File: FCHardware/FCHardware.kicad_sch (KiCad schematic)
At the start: 29 parts, among them J1 USB_B_Mini, P1 USB_C_Plug_USB2.0, Q1 MMBT2222A, Q2 MMBT2222A, SW1 SW_DPST_Custom_PIN, U1 ESP32-WROOM-32, U2 MIC5219-3.3YMM, U3 CP2104, U4 MCP73831-3-OT, U5 MPU-6050, U6 L293D, U7 L293D

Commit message: Added Power and Motor Management, Accelerator
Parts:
- added C10: 0.1uF, symbol Device:C
- added C11: 2.2nF, symbol Device:C
- added J2, J3, J4, J5: Conn_01x02, symbol Connector_Generic:Conn_01x02
- added R8, R9: 0R, symbol Device:R
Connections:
- net GND: now also U5.1 (CLKIN), U5.11 (FSYNC), U5.18 (GND), C10.2, C11.2, R8.2
- net VBUS: now also U5.13 (VDD), U5.8 (VLOGIC), R9.1
- net at U5.10 (REGOUT): now also C10.1
- net INT: now reaches U5.12 (INT)
- net at U5.20 (CPOUT): now also C11.1
- net SCL: now reaches U5.23 (SCL)
- net SDA: now reaches U5.24 (SDA)
- net AUX_SDA: now reaches U5.6 (AUX_DA)
- net AUX_SCL: now reaches U5.7 (AUX_CL)
- net ADD: now reaches U5.9 (AD0)
- net ADD: now also R8.1, R9.2
- new net M1+: J2.1 (Pin_1)
- new net M1-: J2.2 (Pin_2)
- new net M2+: J3.1 (Pin_1)
- new net M2-: J3.2 (Pin_2)
- new net M3+: J4.1 (Pin_1)
- new net M3-: J4.2 (Pin_2)
- new net M4+: J5.1 (Pin_1)
- new net M4-: J5.2 (Pin_2)
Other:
- moved on the sheet: C1, C2, C3, C4, C5, C6, C7, C8, C9, D1, J1, P1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

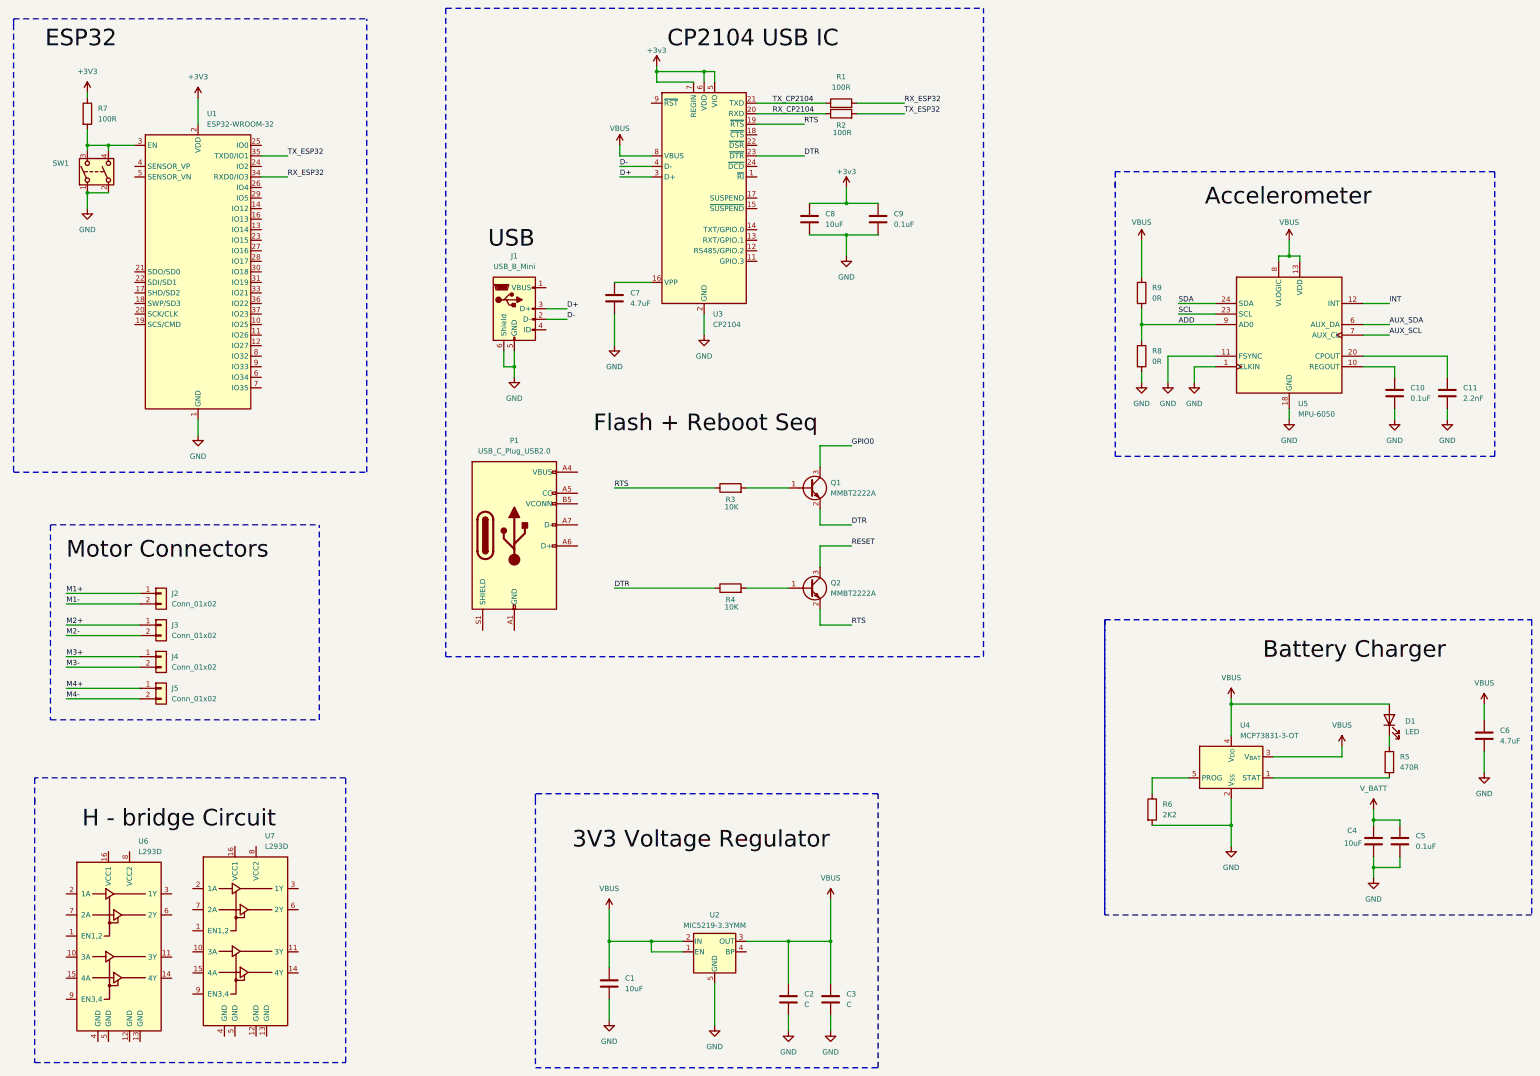
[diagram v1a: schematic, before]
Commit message: Changed main controller to Feather 32 and updated schematics accordingly
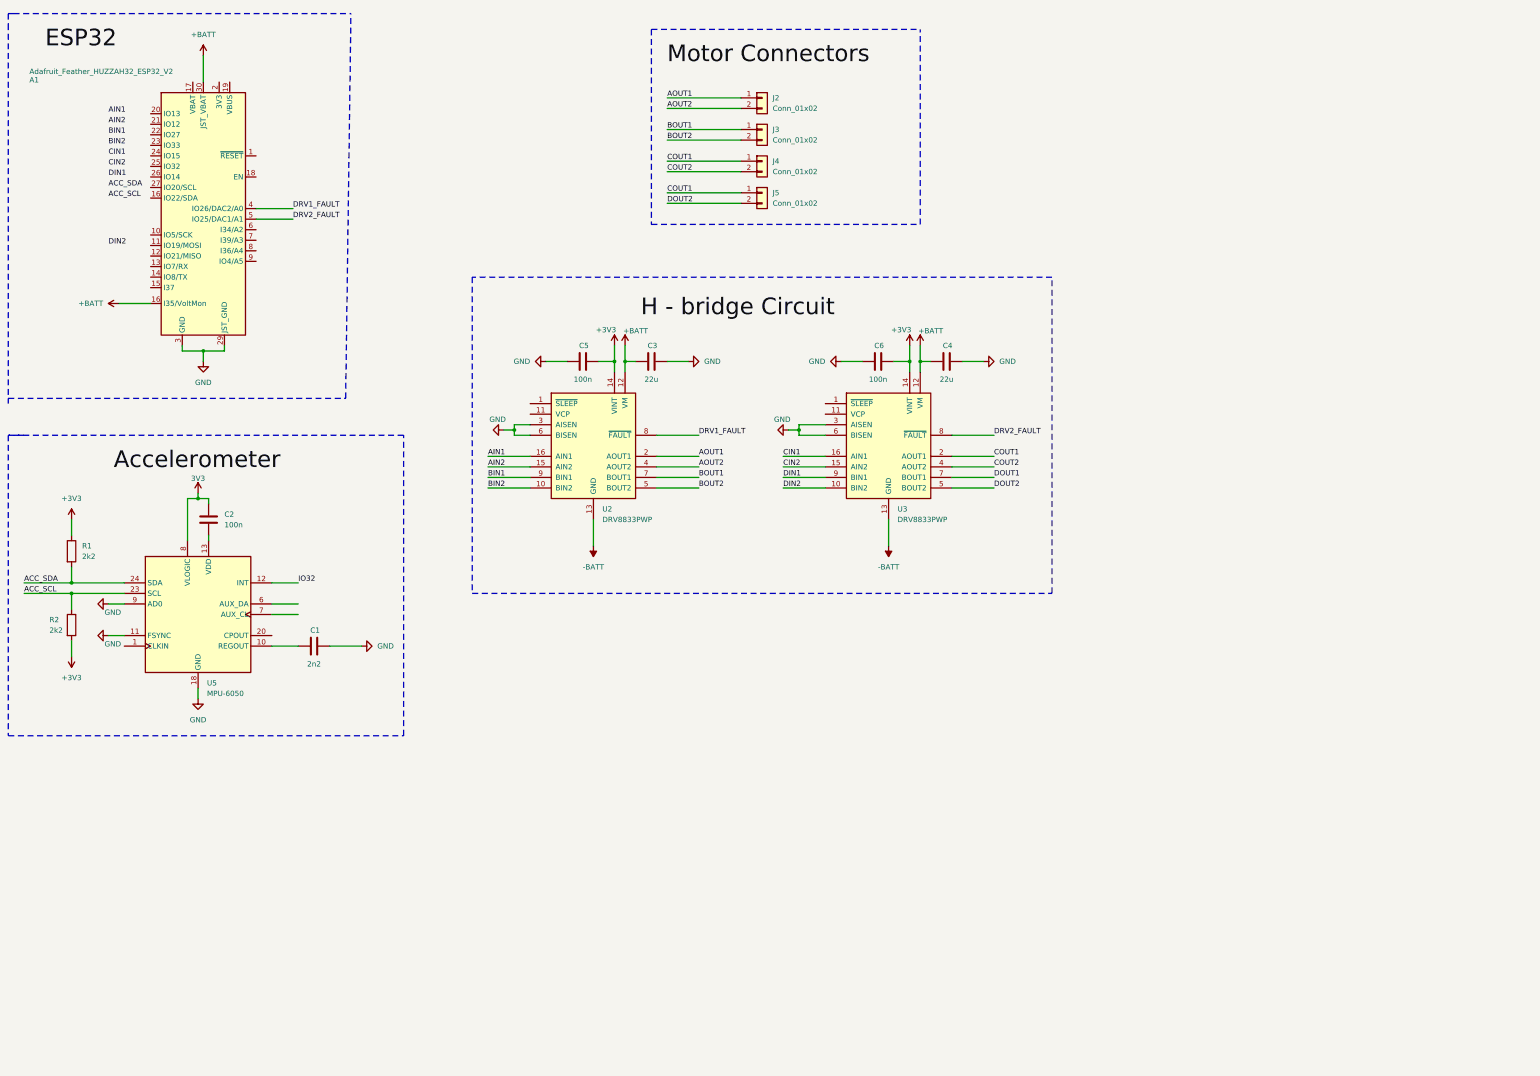
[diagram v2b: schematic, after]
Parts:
- removed C10, C9: 0.1uF, symbol Device:C
- removed C11: 2.2nF, symbol Device:C
- removed C7: 4.7uF, symbol Device:C
- removed C8: 10uF, symbol Device:C
- removed D1: LED, symbol Device:LED
- removed J1: USB_B_Mini, symbol Connector:USB_B_Mini
- removed P1: USB_C_Plug_USB2.0, symbol Connector:USB_C_Plug_USB2.0
- removed Q1, Q2: MMBT2222A, Package_TO_SOT_SMD:SOT-23, symbol Transistor_BJT:MMBT2222A
- removed R3, R4: 10K, symbol Device:R
- removed R5: 470R, symbol Device:R
- removed R6: 2K2, symbol Device:R
- removed R7: 100R, symbol Device:R
- removed R8, R9: 0R, symbol Device:R
- removed SW1: SW_DPST_Custom_PIN, symbol switches:SW_DPST_Custom_PIN
- removed U1: ESP32-WROOM-32, RF_Module:ESP32-WROOM-32, symbol RF_Module:ESP32-WROOM-32
- removed U2: MIC5219-3.3YMM, Package_SO:MSOP-8_3x3mm_P0.65mm, symbol Regulator_Linear:MIC5219-3.3YMM
- removed U3: CP2104, Package_DFN_QFN:QFN-24-1EP_4x4mm_P0.5mm_EP2.6x2.6mm, symbol Interface_USB:CP2104
- removed U4: MCP73831-3-OT, Package_TO_SOT_SMD:SOT-23-5, symbol Battery_Management:MCP73831-3-OT
- removed U6, U7: L293D, Package_DIP:DIP-16_W7.62mm, symbol Driver_Motor:L293D
- added A1: Adafruit_Feather_HUZZAH32_ESP32_V2, Module:Adafruit_Feather, symbol Custom_ESP32_Library:Adafruit_Feather_HUZZAH32_ESP32_v2
- added U2, U3: DRV8833PWP, Package_SO:HTSSOP-16-1EP_4.4x5mm_P0.65mm_EP3x3mm, symbol Driver_Motor:DRV8833PWP
- C1: value 10uF -> 2n2
- C2: value C -> 100n
- C3: value C -> 22u
- C4: value 10uF -> 22u
- C5: value 0.1uF -> 100n
- C6: value 4.7uF -> 100n
- R1, R2: value 100R -> 2k2
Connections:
- net ADD is gone; now on net GND: U5.9 (AD0)
- net M4+ is gone; now on net COUT1: J5.1 (Pin_1)
- net SCL is gone; now on net ACC_SCL: U5.23 (SCL)
- net SDA is gone; now on net ACC_SDA: U5.24 (SDA)
- net TX_CP2104 is gone; now on net +3V3: R1.1
- net TX_ESP32 is gone; now on net +3V3: R2.2
- net +3V3: now also C5.2, C6.2, U2.14 (VINT), U3.14 (VINT)
- net GND: now also C5.1, C6.1, A1.29 (JST_GND), A1.3 (GND), U2.3 (AISEN), U2.6 (BISEN), U3.3 (AISEN), U3.6 (BISEN); no longer C2.2, C5.2, C6.2, U5.1 (CLKIN)
- net at U5.10 (REGOUT): now also C1.1
- net AUX_SCL: no longer names the net of U5.7 (AUX_CL)
- net AUX_SDA: no longer names the net of U5.6 (AUX_DA)
- net INT renamed IO32
- net M1+ renamed AOUT1
- net AOUT1: now also U2.2 (AOUT1)
- net M1- renamed AOUT2
- net AOUT2: now also U2.4 (AOUT2)
- net M2+ renamed BOUT1
- net BOUT1: now also U2.7 (BOUT1)
- net M2- renamed BOUT2
- net BOUT2: now also U2.5 (BOUT2)
- net M3+ renamed COUT1
- net COUT1: now also U3.2 (AOUT1)
- net M3- renamed COUT2
- net COUT2: now also U3.4 (AOUT2)
- net M4- renamed DOUT2
- net DOUT2: now also U3.5 (BOUT2)
- net RX_CP2104 renamed ACC_SCL
- net RX_ESP32 renamed ACC_SDA
- removed net VBUS: C1.1, C2.1, C3.1, C6.1, U5.13 (VDD), U5.8 (VLOGIC)
- net V_BATT renamed +BATT
- net +BATT: now also C3.1, A1.16 (I35/VoltMon), A1.30 (JST_VBAT), U2.12 (VM), U3.12 (VM); no longer C5.1
- new net: C2.1, U5.13 (VDD)
- new net -BATT: U2.13 (GND), U2.17 (GND), U3.13 (GND), U3.17 (GND)
- new net 3V3: C2.2, U5.8 (VLOGIC)
- new net AIN1: U2.16 (AIN1)
- new net AIN2: U2.15 (AIN2)
- new net BIN1: U2.9 (BIN1)
- new net BIN2: U2.10 (BIN2)
- new net CIN1: U3.16 (AIN1)
- new net CIN2: U3.15 (AIN2)
- new net DIN1: U3.9 (BIN1)
- new net DIN2: U3.10 (BIN2)
- new net DOUT1: U3.7 (BOUT1)
- new net DRV1_FAULT: A1.4 (IO26/DAC2/A0), U2.8 (~{FAULT})
- new net DRV2_FAULT: A1.5 (IO25/DAC1/A1), U3.8 (~{FAULT})
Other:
- moved on the sheet: J2, J3, J4, J5, U5

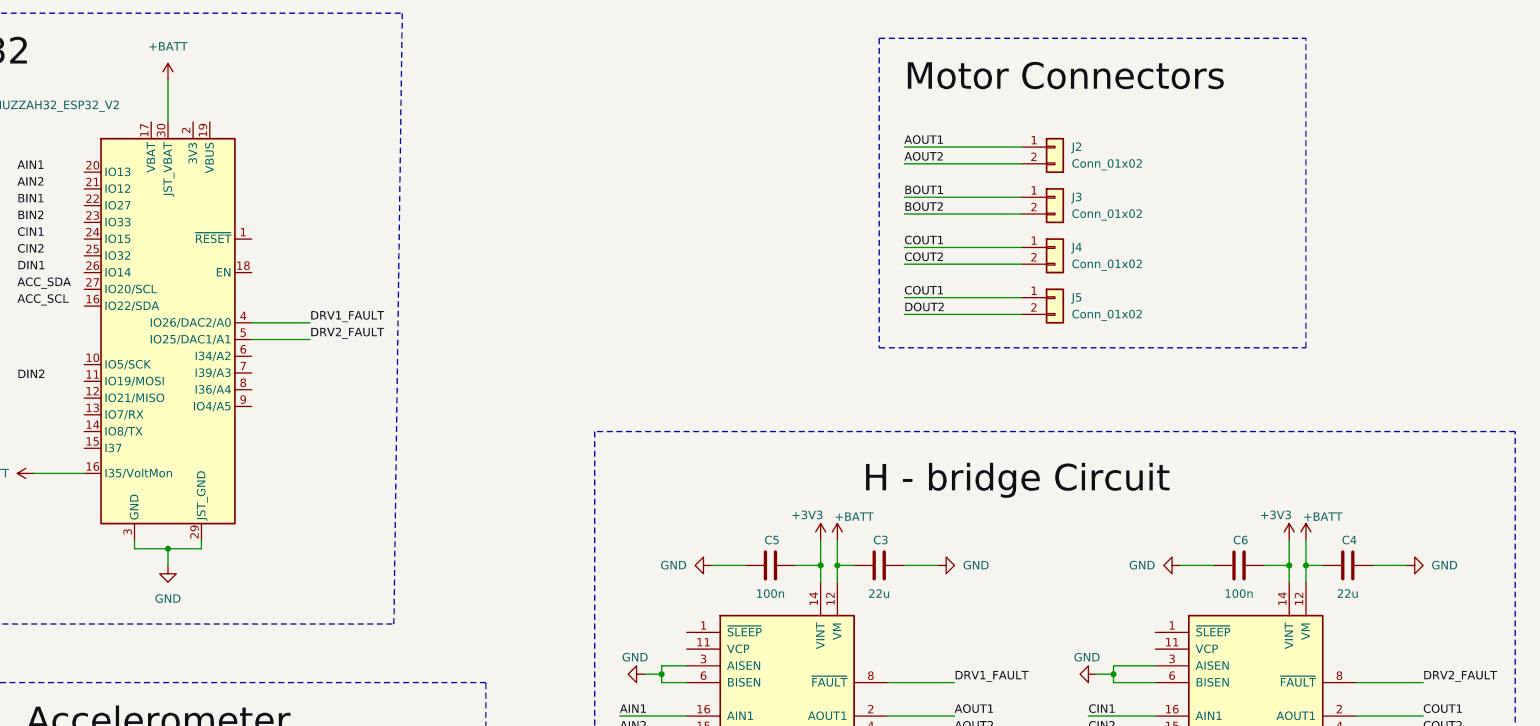
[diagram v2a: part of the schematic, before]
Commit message: Updated configuration to 2S LiPo battery
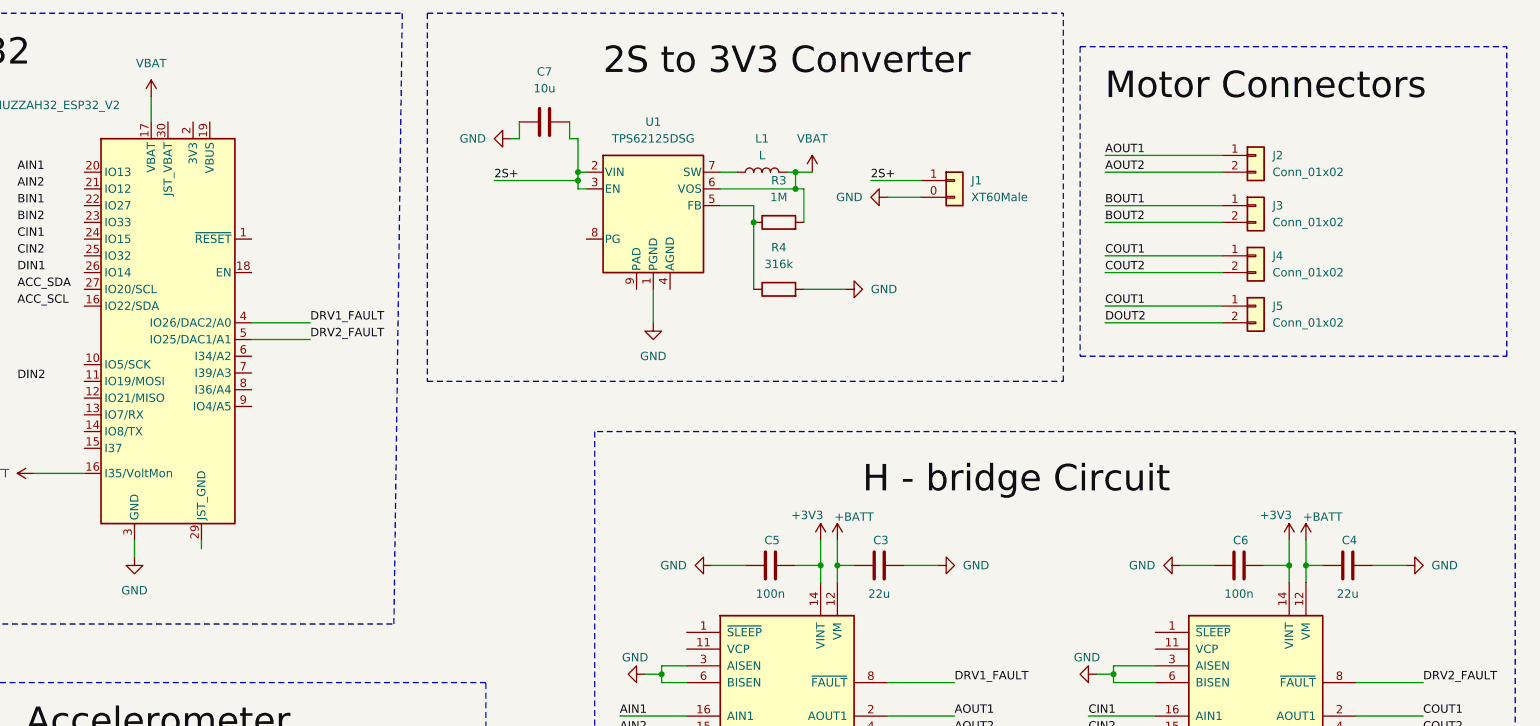
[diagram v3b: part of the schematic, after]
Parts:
- added C7: 10u, symbol Device:C
- added J1: XT60Male, symbol Custom_ESP32_Library:XT60Male
- added L1: L, symbol Device:L
- added R3: 1M, symbol Device:R
- added R4: 316k, symbol Device:R
- added U1: TPS62125DSG, Package_SON:WSON-8-1EP_2x2mm_P0.5mm_EP0.9x1.6mm_ThermalVias, symbol Regulator_Switching:TPS62125DSG
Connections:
- net +BATT: no longer A1.30 (JST_VBAT)
- net GND: now also C7.1, J1.0 (-), R4.2, U1.1 (PGND); no longer A1.29 (JST_GND)
- net VBAT: now reaches A1.17 (VBAT)
- net VBAT: now also L1.2, R3.2, U1.6 (VOS)
- new net: R3.1, R4.1, U1.5 (FB)
- new net: L1.1, U1.7 (SW)
- new net 2S+: C7.2, J1.1 (+), U1.2 (VIN), U1.3 (EN)
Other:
- moved on the sheet: J2, J3, J4, J5

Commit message: Fixed TPS62125DSG power inputs/outputs
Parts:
- added C8: 100u, symbol Device:C
- L1: value L -> 2u2
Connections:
- net 2S+ is gone; now on net VBAT: C7.2, J1.1 (+), U1.2 (VIN), U1.3 (EN)
- net GND: now also C8.1
- net VBAT: now also C8.2; no longer A1.17 (VBAT), L1.2, R3.2, U1.6 (VOS)
- net +5V: now reaches A1.19 (VBUS)
- net +5V: now also L1.2, R3.2, U1.6 (VOS)
